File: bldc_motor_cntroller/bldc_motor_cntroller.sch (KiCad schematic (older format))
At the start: 0 parts

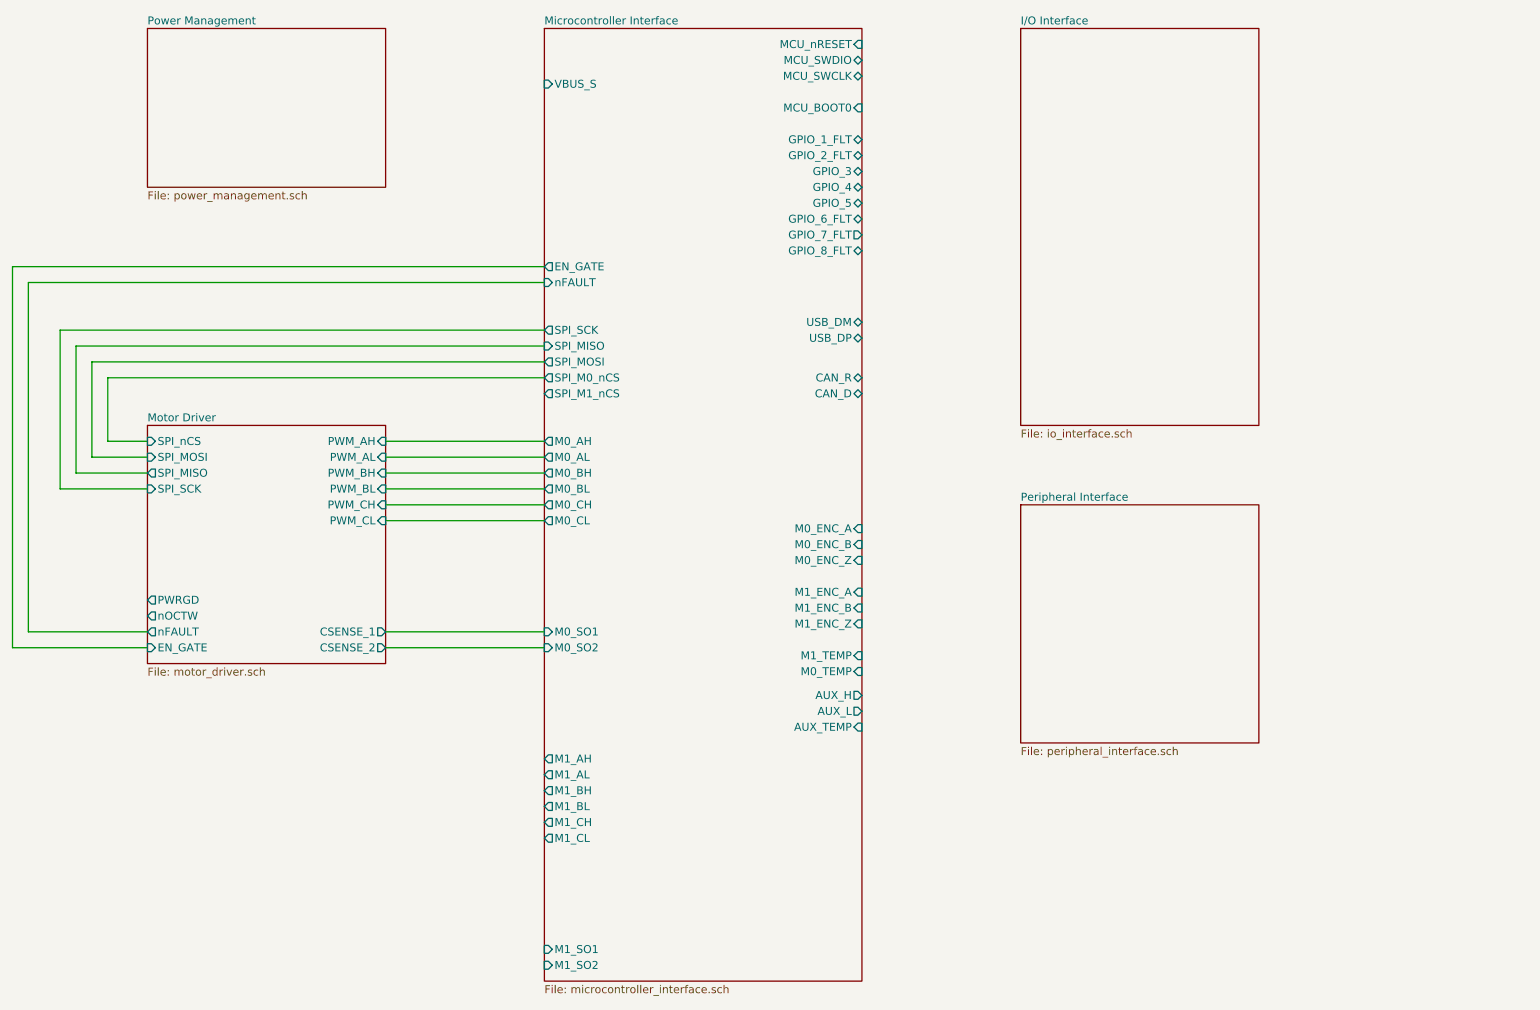
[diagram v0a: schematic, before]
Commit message: finished motor driver interface.
Signed-off-by: azmat bilal <azmat.bilal@outlook.com>
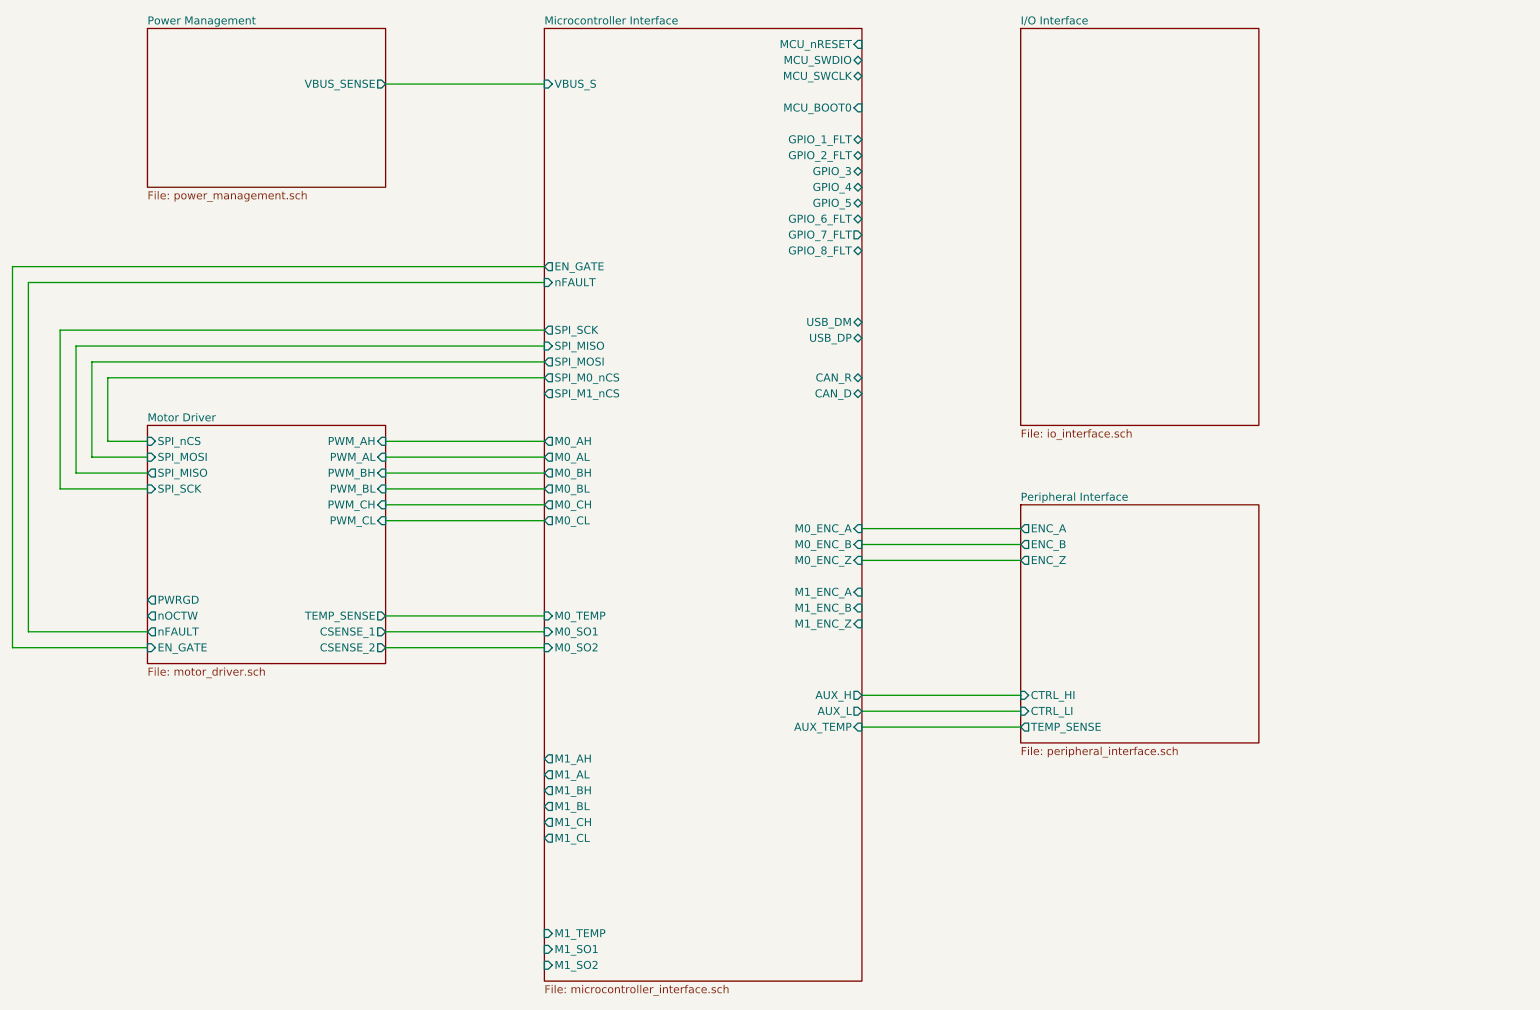
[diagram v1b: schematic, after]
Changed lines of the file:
@@
 F7 "M1_SO1" I L 4500 6800 50
 F8 "GPIO_5" B R 6500 2100 50
-F9 "M0_TEMP" I R 6500 5050 50
+F9 "M0_TEMP" I L 4500 4700 50
 F10 "M1_AH" O L 4500 5600 50
 F11 "M1_BH" O L 4500 5800 50
@@
 F21 "GPIO_3" B R 6500 1900 50
 F22 "GPIO_4" B R 6500 2000 50
-F23 "M1_TEMP" I R 6500 4950 50
+F23 "M1_TEMP" I L 4500 6700 50
 F24 "AUX_TEMP" I R 6500 5400 50
 F25 "VBUS_S" I L 4500 1350 50
@@
 F0 "Power Management" 50
 F1 "power_management.sch" 50
+F2 "VBUS_SENSE" O R 3500 1350 50
 $EndSheet
 $Sheet
@@
 F0 "Peripheral Interface" 50
 F1 "peripheral_interface.sch" 50
+F2 "ENC_A" O L 7500 4150 50
+F3 "ENC_B" O L 7500 4250 50
+F4 "ENC_Z" O L 7500 4350 50
+F5 "CTRL_HI" I L 7500 5200 50
+F6 "CTRL_LI" I L 7500 5300 50
+F7 "TEMP_SENSE" O L 7500 5400 50
 $EndSheet
 Wire Wire Line
@@
 F16 "PWM_AH" I R 3500 3600 50
 F17 "PWM_AL" I R 3500 3700 50
+F18 "TEMP_SENSE" O R 3500 4700 50
 $EndSheet
+Wire Wire Line
+	3500 4700 4500 4700
+Wire Wire Line
+	7500 4150 6500 4150
+Wire Wire Line
+	6500 4250 7500 4250
+Wire Wire Line
+	7500 4350 6500 4350
+Wire Wire Line
+	3500 1350 4500 1350
+Wire Wire Line
+	6500 5200 7500 5200
+Wire Wire Line
+	7500 5300 6500 5300
+Wire Wire Line
+	6500 5400 7500 5400
 $EndSCHEMATC

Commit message: schematic annotation. added bulk caps. moved shunt res to powersheet.
Signed-off-by: azmat bilal <azmat.bilal@outlook.com>
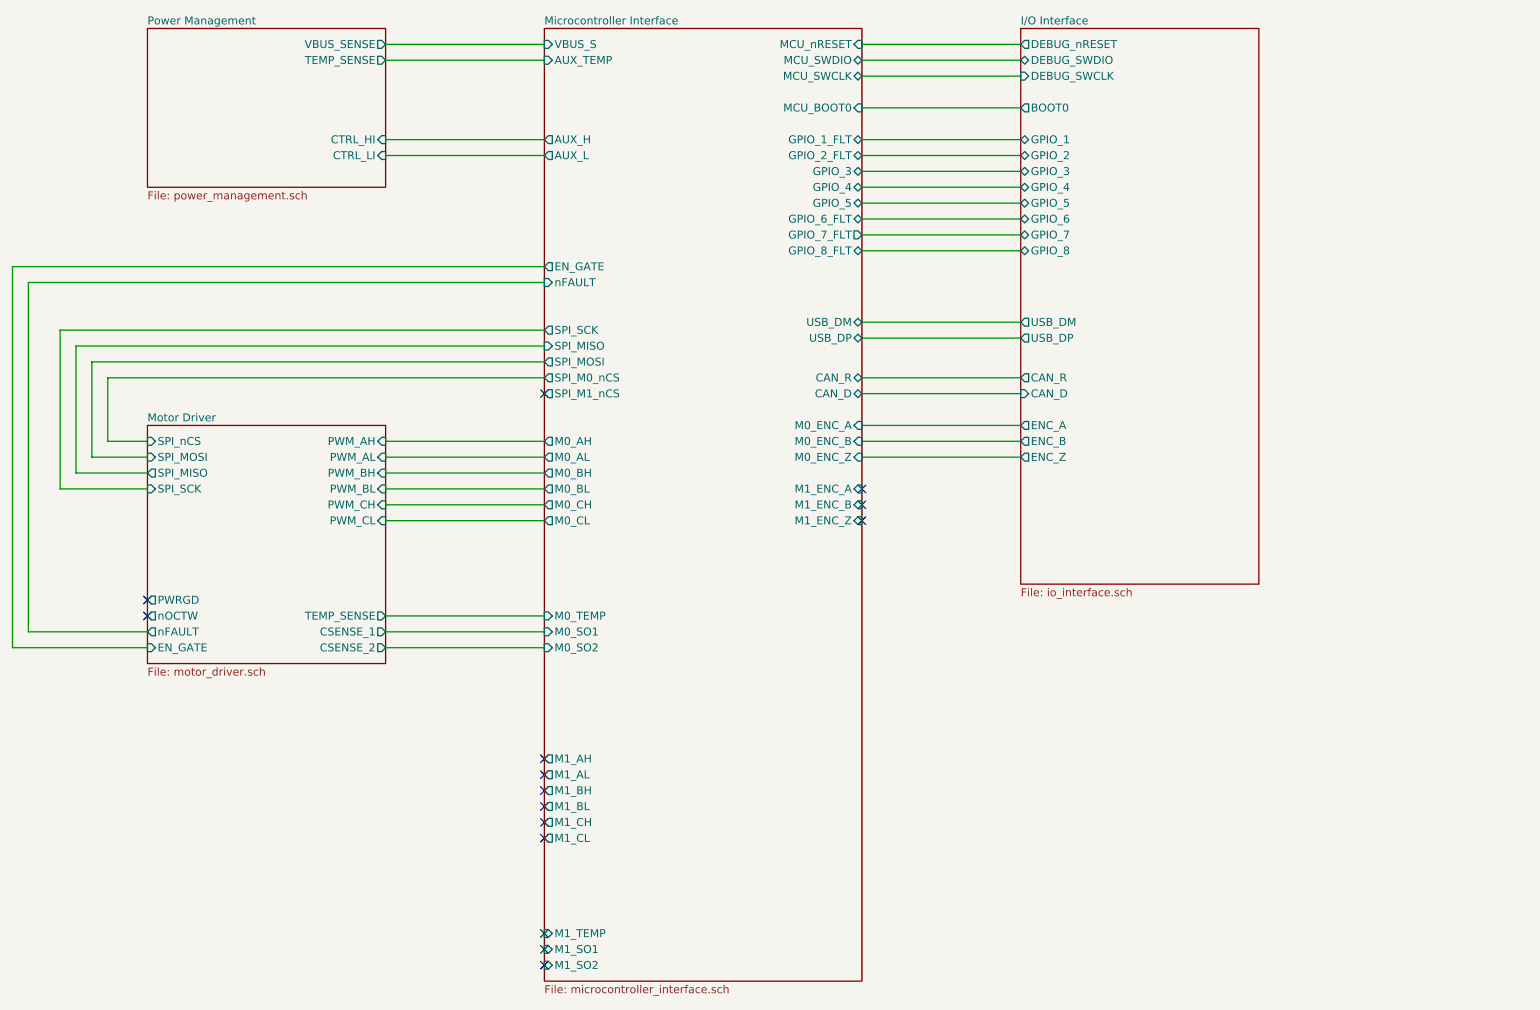
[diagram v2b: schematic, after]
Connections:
- no-connect marks 0 -> 15
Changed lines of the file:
@@
 $Descr A4 11693 8268
 encoding utf-8
-Sheet 1 6
+Sheet 1 5
 Title ""
 Date ""
@@
 $EndDescr
 $Sheet
-S 4500 1000 2000 6000
-U 5E2D91C5
-F0 "Microcontroller Interface" 50
-F1 "microcontroller_interface.sch" 50
-F2 "MCU_nRESET" I R 6500 1100 50
-F3 "MCU_BOOT0" I R 6500 1500 50
-F4 "M0_SO1" I L 4500 4800 50
-F5 "M0_SO2" I L 4500 4900 50
-F6 "M1_SO2" I L 4500 6900 50
-F7 "M1_SO1" I L 4500 6800 50
-F8 "GPIO_5" B R 6500 2100 50
-F9 "M0_TEMP" I L 4500 4700 50
-F10 "M1_AH" O L 4500 5600 50
-F11 "M1_BH" O L 4500 5800 50
-F12 "M1_CH" O L 4500 6000 50
-F13 "M0_ENC_Z" I R 6500 4350 50
-F14 "SPI_SCK" O L 4500 2900 50
-F15 "SPI_MISO" I L 4500 3000 50
-F16 "SPI_MOSI" O L 4500 3100 50
-F17 "SPI_M0_nCS" O L 4500 3200 50
-F18 "SPI_M1_nCS" O L 4500 3300 50
-F19 "GPIO_1_FLT" B R 6500 1700 50
-F20 "GPIO_2_FLT" B R 6500 1800 50
-F21 "GPIO_3" B R 6500 1900 50
-F22 "GPIO_4" B R 6500 2000 50
-F23 "M1_TEMP" I L 4500 6700 50
-F24 "AUX_TEMP" I R 6500 5400 50
-F25 "VBUS_S" I L 4500 1350 50
-F26 "M1_AL" O L 4500 5700 50
-F27 "M0_AH" O L 4500 3600 50
-F28 "M0_BH" O L 4500 3800 50
-F29 "M0_CH" O L 4500 4000 50
-F30 "USB_DM" B R 6500 2850 50
-F31 "USB_DP" B R 6500 2950 50
-F32 "MCU_SWDIO" B R 6500 1200 50
-F33 "MCU_SWCLK" B R 6500 1300 50
-F34 "GPIO_7_FLT" O R 6500 2300 50
-F35 "M1_BL" O L 4500 5900 50
-F36 "M1_CL" O L 4500 6100 50
-F37 "GPIO_6_FLT" B R 6500 2200 50
-F38 "GPIO_8_FLT" B R 6500 2400 50
-F39 "M0_ENC_A" I R 6500 4150 50
-F40 "M0_ENC_B" I R 6500 4250 50
-F41 "M1_ENC_A" I R 6500 4550 50
-F42 "M1_ENC_B" I R 6500 4650 50
-F43 "CAN_R" B R 6500 3200 50
-F44 "CAN_D" B R 6500 3300 50
-F45 "AUX_L" O R 6500 5300 50
-F46 "AUX_H" O R 6500 5200 50
-F47 "EN_GATE" O L 4500 2500 50
-F48 "M0_AL" O L 4500 3700 50
-F49 "M0_BL" O L 4500 3900 50
-F50 "M0_CL" O L 4500 4100 50
-F51 "nFAULT" I L 4500 2600 50
-F52 "M1_ENC_Z" I R 6500 4750 50
-$EndSheet
-$Sheet
-S 7500 1000 1500 2500
+S 7500 1000 1500 3500
 U 5E2D92A8
 F0 "I/O Interface" 50
 F1 "io_interface.sch" 50
+F2 "GPIO_1" B L 7500 1700 50
+F3 "GPIO_2" B L 7500 1800 50
+F4 "GPIO_7" B L 7500 2300 50
+F5 "GPIO_8" B L 7500 2400 50
+F6 "GPIO_3" B L 7500 1900 50
+F7 "GPIO_6" B L 7500 2200 50
+F8 "GPIO_4" B L 7500 2000 50
+F9 "GPIO_5" B L 7500 2100 50
+F10 "DEBUG_SWDIO" B L 7500 1200 50
+F11 "DEBUG_SWCLK" I L 7500 1300 50
+F12 "DEBUG_nRESET" O L 7500 1100 50
+F13 "BOOT0" O L 7500 1500 50
+F14 "USB_DP" O L 7500 2950 50
+F15 "USB_DM" O L 7500 2850 50
+F16 "CAN_D" I L 7500 3300 50
+F17 "CAN_R" O L 7500 3200 50
+F18 "ENC_A" O L 7500 3500 50
+F19 "ENC_B" O L 7500 3600 50
+F20 "ENC_Z" O L 7500 3700 50
 $EndSheet
 $Sheet
@@
 F0 "Power Management" 50
 F1 "power_management.sch" 50
-F2 "VBUS_SENSE" O R 3500 1350 50
-$EndSheet
-$Sheet
-S 7500 4000 1500 1500
-U 5E377C6C
-F0 "Peripheral Interface" 50
-F1 "peripheral_interface.sch" 50
-F2 "ENC_A" O L 7500 4150 50
-F3 "ENC_B" O L 7500 4250 50
-F4 "ENC_Z" O L 7500 4350 50
-F5 "CTRL_HI" I L 7500 5200 50
-F6 "CTRL_LI" I L 7500 5300 50
-F7 "TEMP_SENSE" O L 7500 5400 50
+F2 "VBUS_SENSE" O R 3500 1100 50
+F3 "CTRL_HI" I R 3500 1700 50
+F4 "CTRL_LI" I R 3500 1800 50
+F5 "TEMP_SENSE" O R 3500 1200 50
 $EndSheet
 Wire Wire Line
@@
 	3500 4700 4500 4700
 Wire Wire Line
-	7500 4150 6500 4150
-Wire Wire Line
-	6500 4250 7500 4250
-Wire Wire Line
-	7500 4350 6500 4350
-Wire Wire Line
-	3500 1350 4500 1350
-Wire Wire Line
-	6500 5200 7500 5200
-Wire Wire Line
-	7500 5300 6500 5300
-Wire Wire Line
-	6500 5400 7500 5400
+	6500 1100 7500 1100
+Wire Wire Line
+	7500 1200 6500 1200
+Wire Wire Line
+	6500 1300 7500 1300
+Wire Wire Line
+	6500 1700 7500 1700
+Wire Wire Line
+	7500 1800 6500 1800
+Wire Wire Line
+	6500 1900 7500 1900
+Wire Wire Line
+	7500 2000 6500 2000
+Wire Wire Line
+	6500 2100 7500 2100
+Wire Wire Line
+	7500 2200 6500 2200
+Wire Wire Line
+	6500 2300 7500 2300
+Wire Wire Line
+	7500 2400 6500 2400
+Wire Wire Line
+	7500 1500 6500 1500
+Wire Wire Line
+	6500 2850 7500 2850
+Wire Wire Line
+	7500 2950 6500 2950
+Wire Wire Line
+	6500 3200 7500 3200
+Wire Wire Line
+	7500 3300 6500 3300
+$Sheet
+S 4500 1000 2000 6000
+U 5E2D91C5
+F0 "Microcontroller Interface" 50
+F1 "microcontroller_interface.sch" 50
+F2 "MCU_nRESET" I R 6500 1100 50
+F3 "MCU_BOOT0" I R 6500 1500 50
+F4 "M0_SO1" I L 4500 4800 50
+F5 "M0_SO2" I L 4500 4900 50
+F6 "M1_SO2" I L 4500 6900 50
+F7 "M1_SO1" I L 4500 6800 50
+F8 "GPIO_5" B R 6500 2100 50
+F9 "M0_TEMP" I L 4500 4700 50
+F10 "M1_AH" O L 4500 5600 50
+F11 "M1_BH" O L 4500 5800 50
+F12 "M1_CH" O L 4500 6000 50
+F13 "M0_ENC_Z" I R 6500 3700 50
+F14 "SPI_SCK" O L 4500 2900 50
+F15 "SPI_MISO" I L 4500 3000 50
+F16 "SPI_MOSI" O L 4500 3100 50
+F17 "SPI_M0_nCS" O L 4500 3200 50
+F18 "SPI_M1_nCS" O L 4500 3300 50
+F19 "GPIO_1_FLT" B R 6500 1700 50
+F20 "GPIO_2_FLT" B R 6500 1800 50
+F21 "GPIO_3" B R 6500 1900 50
+F22 "GPIO_4" B R 6500 2000 50
+F23 "M1_TEMP" I L 4500 6700 50
+F24 "AUX_TEMP" I L 4500 1200 50
+F25 "VBUS_S" I L 4500 1100 50
+F26 "M1_AL" O L 4500 5700 50
+F27 "M0_AH" O L 4500 3600 50
+F28 "M0_BH" O L 4500 3800 50
+F29 "M0_CH" O L 4500 4000 50
+F30 "USB_DM" B R 6500 2850 50
+F31 "USB_DP" B R 6500 2950 50
+F32 "MCU_SWDIO" B R 6500 1200 50
+F33 "MCU_SWCLK" B R 6500 1300 50
+F34 "GPIO_7_FLT" O R 6500 2300 50
+F35 "M1_BL" O L 4500 5900 50
+F36 "M1_CL" O L 4500 6100 50
+F37 "GPIO_6_FLT" B R 6500 2200 50
+F38 "GPIO_8_FLT" B R 6500 2400 50
+F39 "M0_ENC_A" I R 6500 3500 50
+F40 "M0_ENC_B" I R 6500 3600 50
+F41 "M1_ENC_A" I R 6500 3900 50
+F42 "M1_ENC_B" I R 6500 4000 50
+F43 "CAN_R" B R 6500 3200 50
+F44 "CAN_D" B R 6500 3300 50
+F45 "AUX_L" O L 4500 1800 50
+F46 "AUX_H" O L 4500 1700 50
+F47 "EN_GATE" O L 4500 2500 50
+F48 "M0_AL" O L 4500 3700 50
+F49 "M0_BL" O L 4500 3900 50
+F50 "M0_CL" O L 4500 4100 50
+F51 "nFAULT" I L 4500 2600 50
+F52 "M1_ENC_Z" I R 6500 4100 50
+$EndSheet
+Wire Wire Line
+	6500 3500 7500 3500
+Wire Wire Line
+	7500 3600 6500 3600
+Wire Wire Line
+	6500 3700 7500 3700
+Wire Wire Line
+	3500 1100 4500 1100
+Wire Wire Line
+	4500 1200 3500 1200
+Wire Wire Line
+	3500 1700 4500 1700
+Wire Wire Line
+	3500 1800 4500 1800
+NoConn ~ 6500 3900
+NoConn ~ 6500 4000
+NoConn ~ 6500 4100
+NoConn ~ 4500 5600
+NoConn ~ 4500 5700
+NoConn ~ 4500 5800
+NoConn ~ 4500 5900
+NoConn ~ 4500 6000
+NoConn ~ 4500 6100
+NoConn ~ 4500 6700
+NoConn ~ 4500 6800
+NoConn ~ 4500 6900
+NoConn ~ 4500 3300
+NoConn ~ 2000 4700
+NoConn ~ 2000 4600
 $EndSCHEMATC

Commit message: added heatsink model in the design
Signed-off-by: azmat bilal <azmat.bilal@outlook.com>
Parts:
- added H1, H2: MountingHole_Pad, MountingHole:MountingHole_2.2mm_M2_ISO7380_Pad, symbol Mechanical:MountingHole_Pad
- added HS1, HS2, HS3: Heatsink, bldc_motor_cntroller:heatsink14x14x6, symbol Mechanical:Heatsink
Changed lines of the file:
@@
 NoConn ~ 2000 4700
 NoConn ~ 2000 4600
+$Comp
+L Mechanical:MountingHole_Pad H1
+U 1 1 5E43C932
+P 7850 5850
+F 0 "H1" H 7950 5853 50  0000 L CNN
+F 1 "MountingHole_Pad" H 7950 5808 50  0001 L CNN
+F 2 "MountingHole:MountingHole_2.2mm_M2_ISO7380_Pad" H 7850 5850 50  0001 C CNN
+F 3 "~" H 7850 5850 50  0001 C CNN
+	1    7850 5850
+	1    0    0    -1
+$EndComp
+$Comp
+L Mechanical:MountingHole_Pad H2
+U 1 1 5E4423C1
+P 8200 5850
+F 0 "H2" H 8300 5853 50  0000 L CNN
+F 1 "MountingHole_Pad" H 8300 5808 50  0001 L CNN
+F 2 "MountingHole:MountingHole_2.2mm_M2_ISO7380_Pad" H 8200 5850 50  0001 C CNN
+F 3 "~" H 8200 5850 50  0001 C CNN
+	1    8200 5850
+	1    0    0    -1
+$EndComp
+$Comp
+L Mechanical:Heatsink HS1
+U 1 1 5E48DBFB
+P 8850 5950
+F 0 "HS1" H 8992 6071 50  0000 L CNN
+F 1 "Heatsink" H 8992 5980 50  0000 L CNN
+F 2 "bldc_motor_cntroller:heatsink14x14x6" H 8862 5950 50  0001 C CNN
+F 3 "~" H 8862 5950 50  0001 C CNN
+	1    8850 5950
+	1    0    0    -1
+$EndComp
+$Comp
+L Mechanical:Heatsink HS2
+U 1 1 5E4936A1
+P 9500 5950
+F 0 "HS2" H 9642 6071 50  0000 L CNN
+F 1 "Heatsink" H 9642 5980 50  0000 L CNN
+F 2 "bldc_motor_cntroller:heatsink14x14x6" H 9512 5950 50  0001 C CNN
+F 3 "~" H 9512 5950 50  0001 C CNN
+	1    9500 5950
+	1    0    0    -1
+$EndComp
+$Comp
+L Mechanical:Heatsink HS3
+U 1 1 5E49388C
+P 10150 5950
+F 0 "HS3" H 10292 6071 50  0000 L CNN
+F 1 "Heatsink" H 10292 5980 50  0000 L CNN
+F 2 "bldc_motor_cntroller:heatsink14x14x6" H 10162 5950 50  0001 C CNN
+F 3 "~" H 10162 5950 50  0001 C CNN
+	1    10150 5950
+	1    0    0    -1
+$EndComp
 $EndSCHEMATC

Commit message: improved BOM
Signed-off-by: azmat bilal <azmat.bilal@outlook.com>
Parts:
- H1, H2, HS1, HS2, HS3: MPN (none) -> -
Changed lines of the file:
@@
 F 2 "MountingHole:MountingHole_2.2mm_M2_ISO7380_Pad" H 7850 5850 50  0001 C CNN
 F 3 "~" H 7850 5850 50  0001 C CNN
+F 4 "-" H 7850 5850 50  0001 C CNN "MPN"
 	1    7850 5850
 	1    0    0    -1
@@
 F 2 "MountingHole:MountingHole_2.2mm_M2_ISO7380_Pad" H 8200 5850 50  0001 C CNN
 F 3 "~" H 8200 5850 50  0001 C CNN
+F 4 "-" H 8200 5850 50  0001 C CNN "MPN"
 	1    8200 5850
 	1    0    0    -1
@@
 F 2 "bldc_motor_cntroller:heatsink14x14x6" H 8862 5950 50  0001 C CNN
 F 3 "~" H 8862 5950 50  0001 C CNN
+F 4 "-" H 8850 5950 50  0001 C CNN "MPN"
 	1    8850 5950
 	1    0    0    -1
@@
 F 2 "bldc_motor_cntroller:heatsink14x14x6" H 9512 5950 50  0001 C CNN
 F 3 "~" H 9512 5950 50  0001 C CNN
+F 4 "-" H 9500 5950 50  0001 C CNN "MPN"
 	1    9500 5950
 	1    0    0    -1
@@
 F 2 "bldc_motor_cntroller:heatsink14x14x6" H 10162 5950 50  0001 C CNN
 F 3 "~" H 10162 5950 50  0001 C CNN
+F 4 "-" H 10150 5950 50  0001 C CNN "MPN"
 	1    10150 5950
 	1    0    0    -1
